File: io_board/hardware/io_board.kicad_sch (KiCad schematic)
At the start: 28 parts, among them J1 8bit_thing_bus_connector, J2 greenpak_i2c, J3 greenpak_i2c, J4 Mini-DIN-6, J5 greenpak_i2c, J6 Micro_SD_Card_Det1, U1 SLG46826G, U2 W65C22, U3 SLG46826G, U4 74AHCT595, U5 SLG46826G, U6 TLV73333PDBV

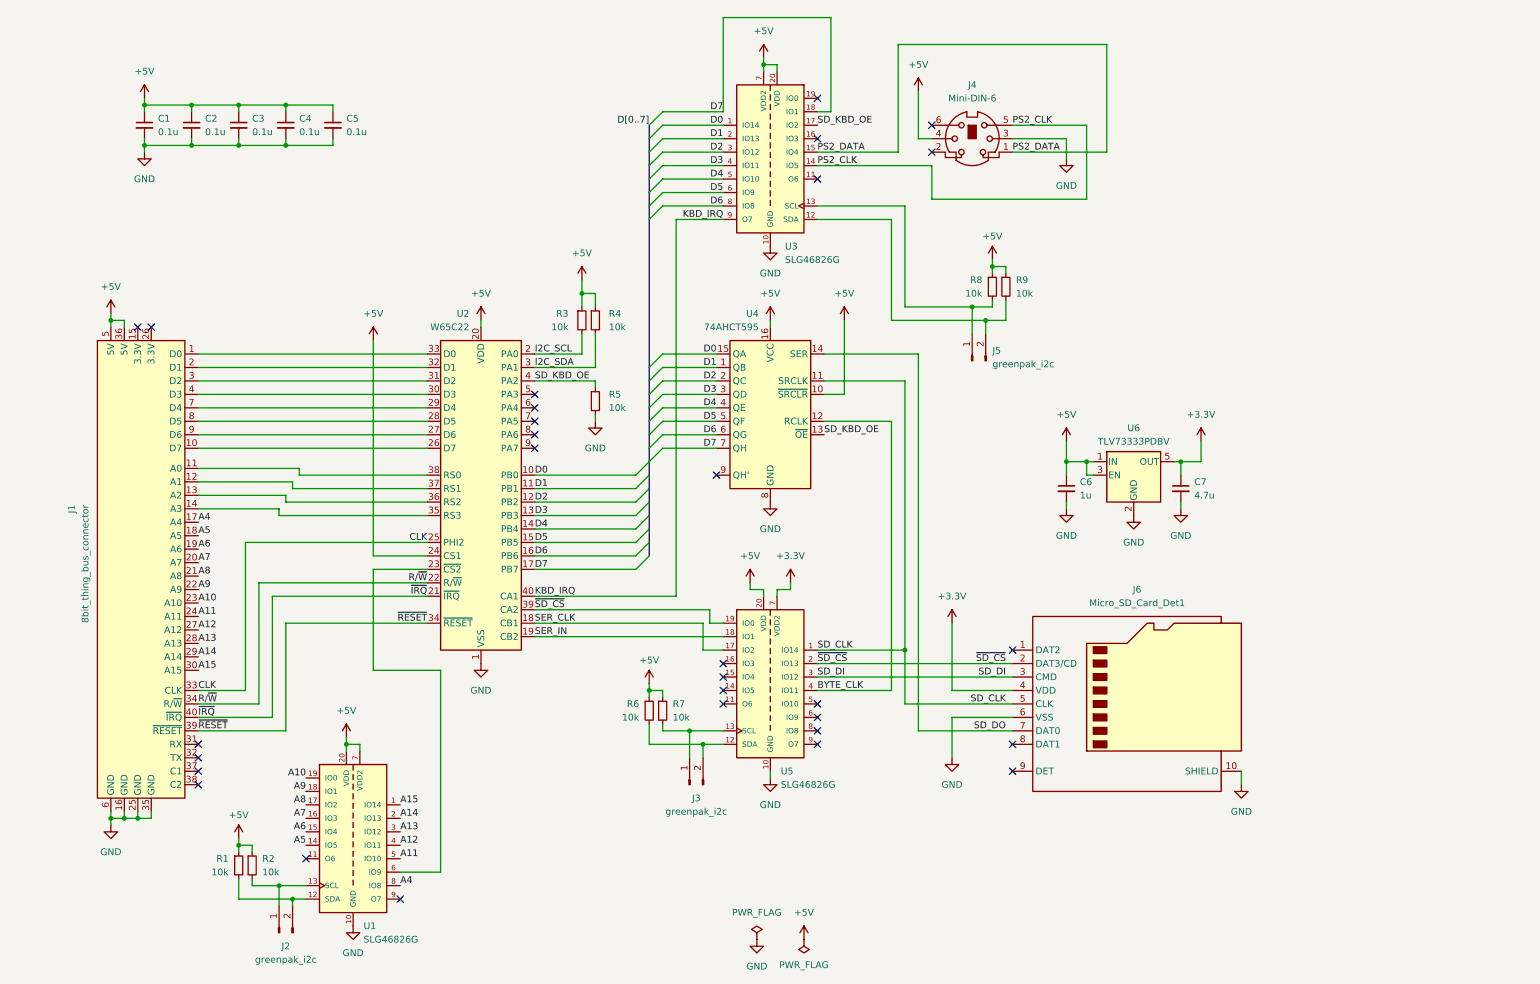
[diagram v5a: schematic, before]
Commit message: Mostly routed IO board
It's still missing:
- An i2c timer
- All the sanity checks
- Making all GreenPAK code match the schematic. Many pins were moved for easier
  routing.
- Aligning the PS2 port with other ports on other boards.
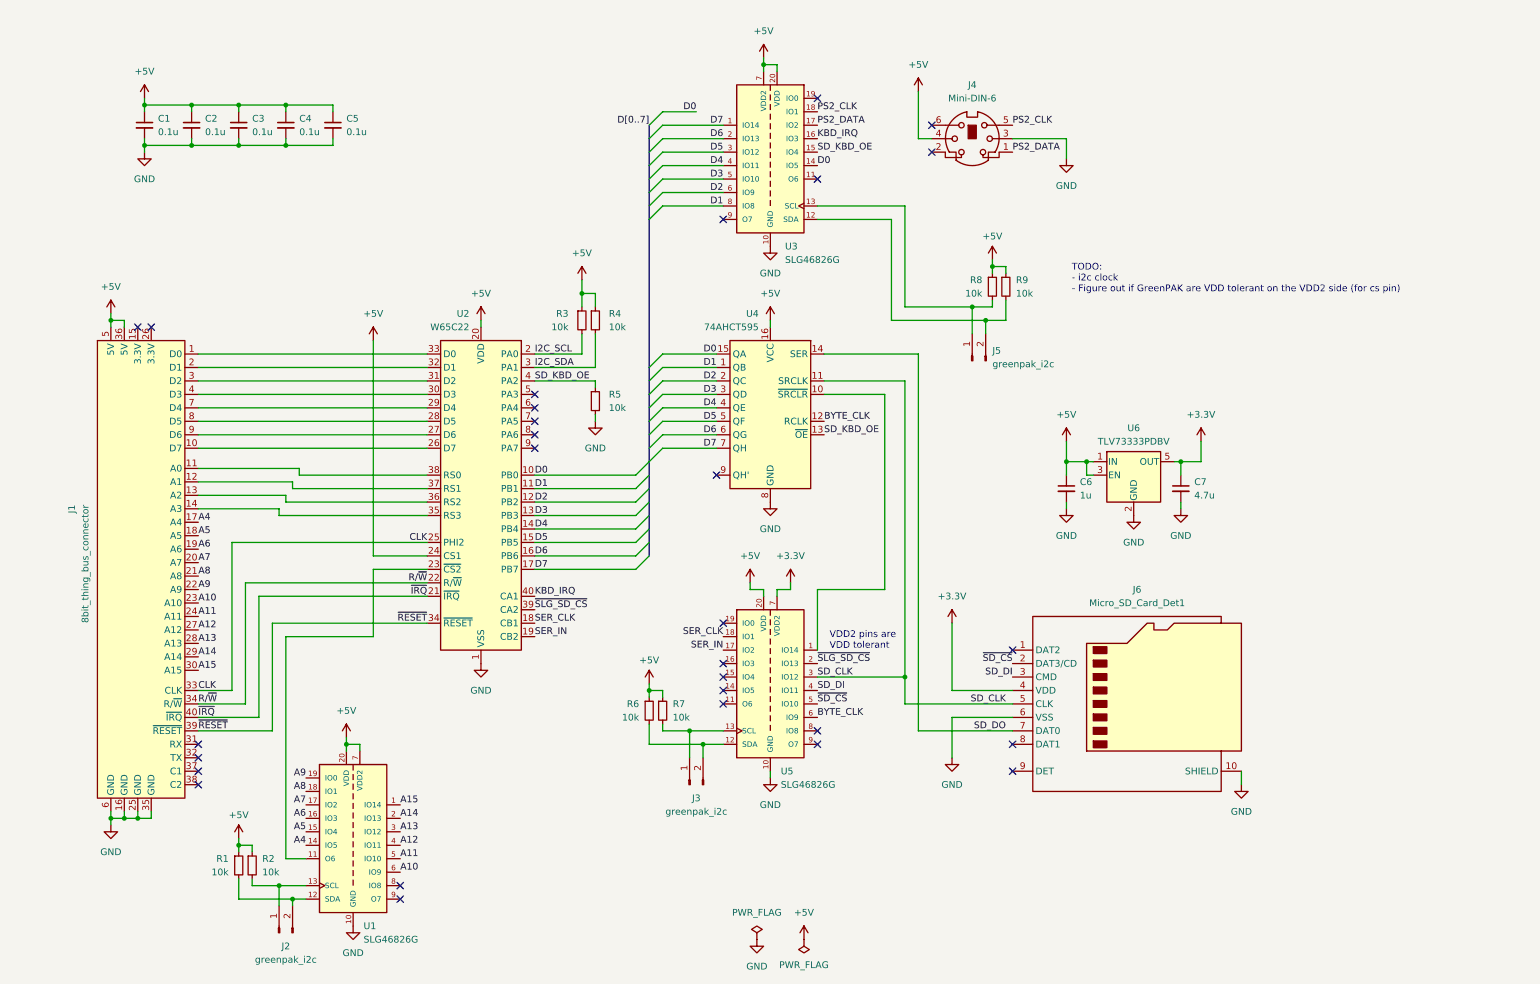
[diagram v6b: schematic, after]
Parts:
- C1, C2, C3, C4, C5, C6, C7: footprint (none) -> Capacitor_SMD:C_0805_2012Metric_Pad1.18x1.45mm_HandSolder
- J4: footprint (none) -> imported_footprints:KMDGX6SBS
- J6: footprint (none) -> Connector_Card:microSD_HC_Hirose_DM3D-SF
- R3, R4, R5: footprint (none) -> Resistor_SMD:R_0805_2012Metric_Pad1.20x1.40mm_HandSolder
- U4: footprint (none) -> Package_SO:TSSOP-16_4.4x5mm_P0.65mm
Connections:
- net +5V: no longer U4.10 (~{SRCLR})
- net A10: now also U1.6 (IO9); no longer U1.19 (IO0)
- net A4: now also U1.14 (IO5); no longer U1.8 (IO8)
- net A5: now also U1.15 (IO4); no longer U1.14 (IO5)
- net A6: now also U1.16 (IO3); no longer U1.15 (IO4)
- net A7: now also U1.17 (IO2); no longer U1.16 (IO3)
- net A8: now also U1.18 (IO1); no longer U1.17 (IO2)
- net A9: now also U1.19 (IO0); no longer U1.18 (IO1)
- net BYTE_CLK: now also U5.6 (IO9); no longer U5.4 (IO11)
- net D0: now also U3.14 (IO5); no longer U3.1 (IO14)
- net D1: now also U3.8 (IO8); no longer U3.2 (IO13)
- net D2: now also U3.6 (IO9); no longer U3.3 (IO12)
- net D3: now also U3.5 (IO10); no longer U3.4 (IO11)
- net D4: now also U3.4 (IO11); no longer U3.5 (IO10)
- net D5: now also U3.3 (IO12); no longer U3.6 (IO9)
- net D6: now also U3.2 (IO13); no longer U3.8 (IO8)
- net D7: now also U3.1 (IO14); no longer U3.18 (IO1)
- net KBD_IRQ: now also U3.16 (IO3); no longer U3.9 (O7)
- net PS2_CLK: now also U3.18 (IO1); no longer U3.14 (IO5)
- net PS2_DATA: now also U3.17 (IO2); no longer U3.15 (IO4)
- net SD_CLK: now also U5.3 (IO12); no longer U5.1 (IO14)
- net SD_DI: now also U5.4 (IO11); no longer U5.3 (IO12)
- net SD_KBD_OE: now also U3.15 (IO4); no longer U3.17 (IO2)
- net SER_CLK: now also U5.18 (IO1); no longer U5.17 (IO2)
- net SER_IN: now also U5.17 (IO2); no longer U5.18 (IO1)
- net ~{SD_CS}: now also U5.5 (IO10); no longer U2.39 (CA2), U5.19 (IO0), U5.2 (IO13)
- net at U2.23 (~{CS2}): now also U1.11 (O6); no longer U1.6 (IO9)
- new net: U4.10 (~{SRCLR}), U5.1 (IO14)
- new net ~{SLG_SD_CS}: U2.39 (CA2), U5.2 (IO13)
- no-connect marks 30 -> 29
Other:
- note added: "TODO: - i2c clock - Figure out if GreenPAK are VDD tolerant on the VDD2 side (for cs pin)"
- note added: "VDD2 pins are VDD tolerant"

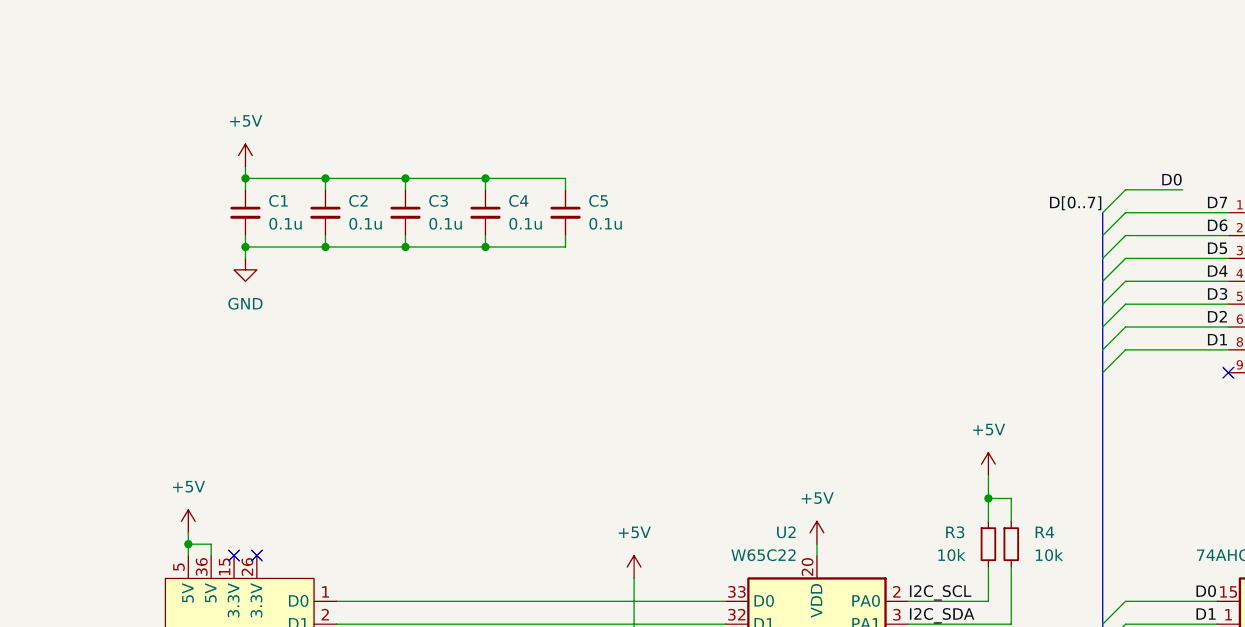
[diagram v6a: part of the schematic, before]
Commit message: Route more of the io board
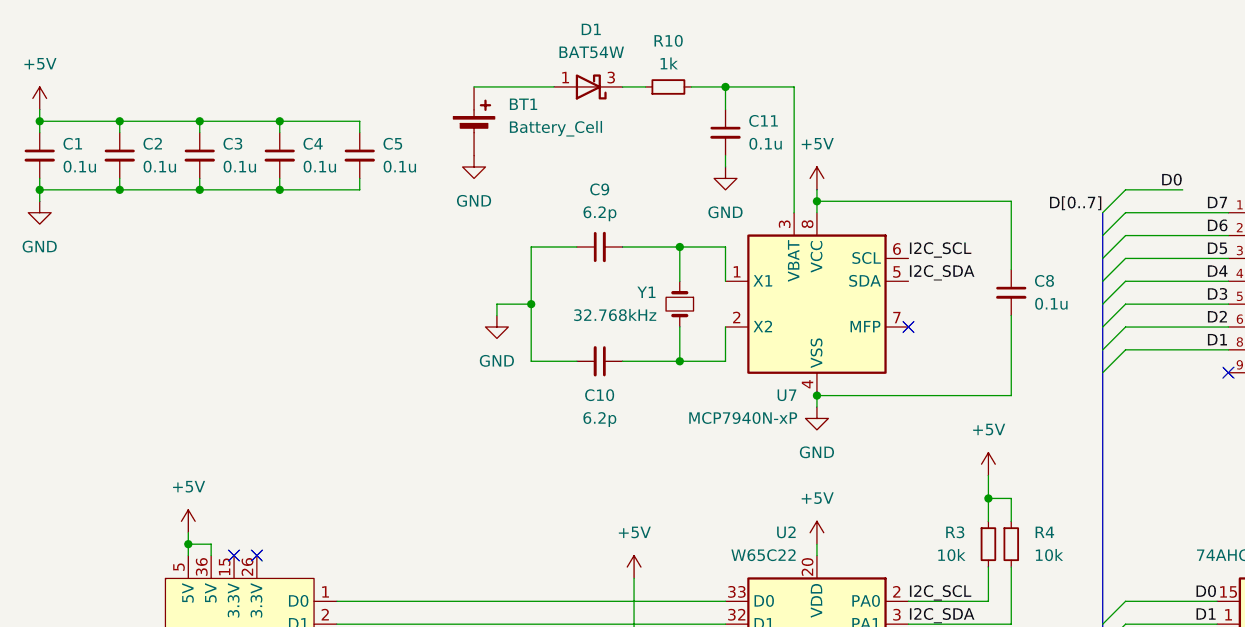
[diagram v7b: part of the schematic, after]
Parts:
- added BT1: Battery_Cell, Battery:BatteryHolder_MPD_BC2003_1x2032, symbol Device:Battery_Cell
- added C10, C9: 6.2p, Capacitor_SMD:C_0805_2012Metric_Pad1.18x1.45mm_HandSolder, symbol Device:C_Small
- added C11, C8: 0.1u, Capacitor_SMD:C_0805_2012Metric_Pad1.18x1.45mm_HandSolder, symbol Device:C_Small
- added D1: BAT54W, Package_TO_SOT_SMD:SOT-323_SC-70, symbol Diode:BAT54W
- added R10: 1k, Resistor_SMD:R_0805_2012Metric_Pad1.20x1.40mm_HandSolder, symbol Device:R_Small
- added U7: MCP7940N-xP, Package_DIP:DIP-8_W7.62mm, symbol Timer_RTC:MCP7940N-xP
- added Y1: 32.768kHz, Crystal:Crystal_C26-LF_D2.1mm_L6.5mm_Horizontal, symbol Device:Crystal_Small
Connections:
- net +5V: now also C8.1, U7.8 (VCC)
- net GND: now also BT1.2 (-), C10.2, C11.2, C8.2, C9.1, U7.4 (VSS)
- net I2C_SCL: now also U7.6 (SCL)
- net I2C_SDA: now also U7.5 (SDA)
- new net: C9.2, U7.1 (X1), Y1.1
- new net: C10.1, U7.2 (X2), Y1.2
- new net: D1.3 (K), R10.1
- new net: C11.1, R10.2, U7.3 (VBAT)
- new net: BT1.1 (+), D1.1 (A)
- no-connect marks 29 -> 30
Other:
- moved on the sheet: C1, C2, C3, C4, C5
